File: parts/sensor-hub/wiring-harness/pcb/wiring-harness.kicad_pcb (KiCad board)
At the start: 2 copper layers, 95.7 x 51.7 mm, 20 parts, among them J1 Conn_01x01_Shielded

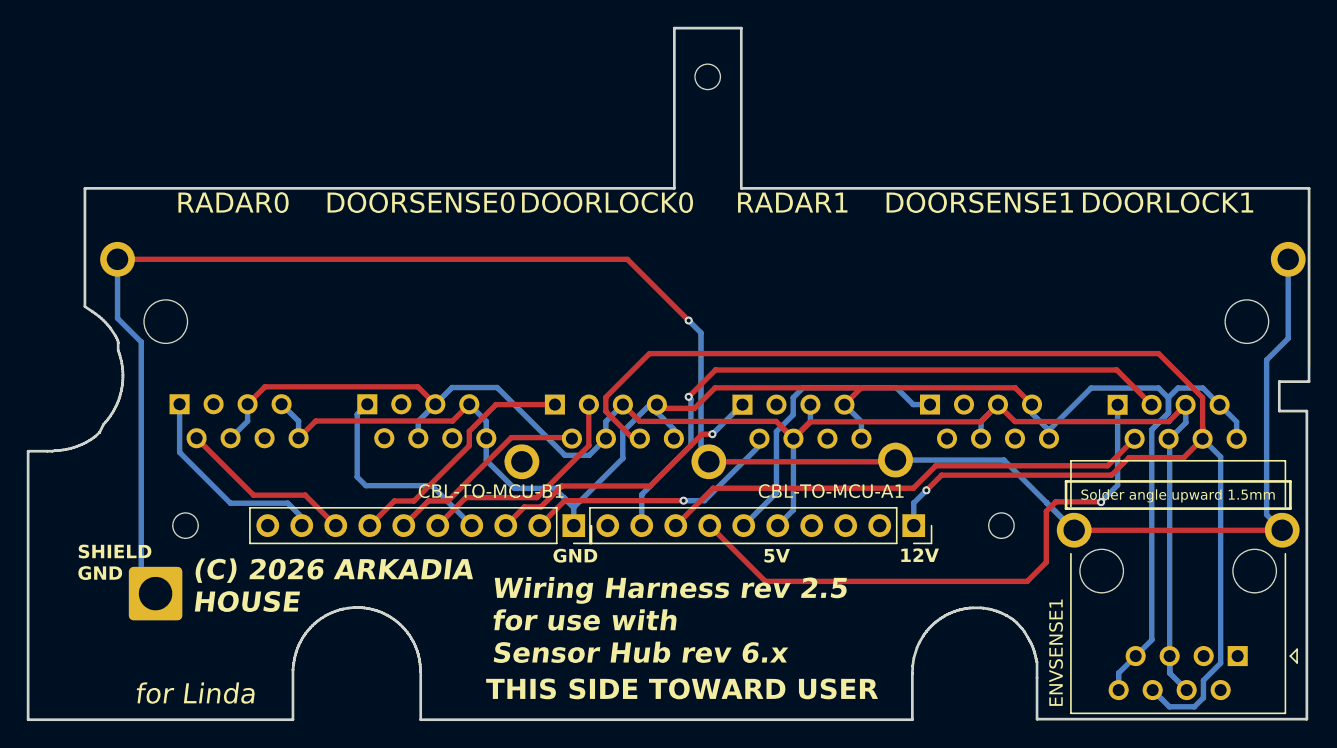
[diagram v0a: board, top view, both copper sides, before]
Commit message: tweak pcb layout to strengthen the supports.
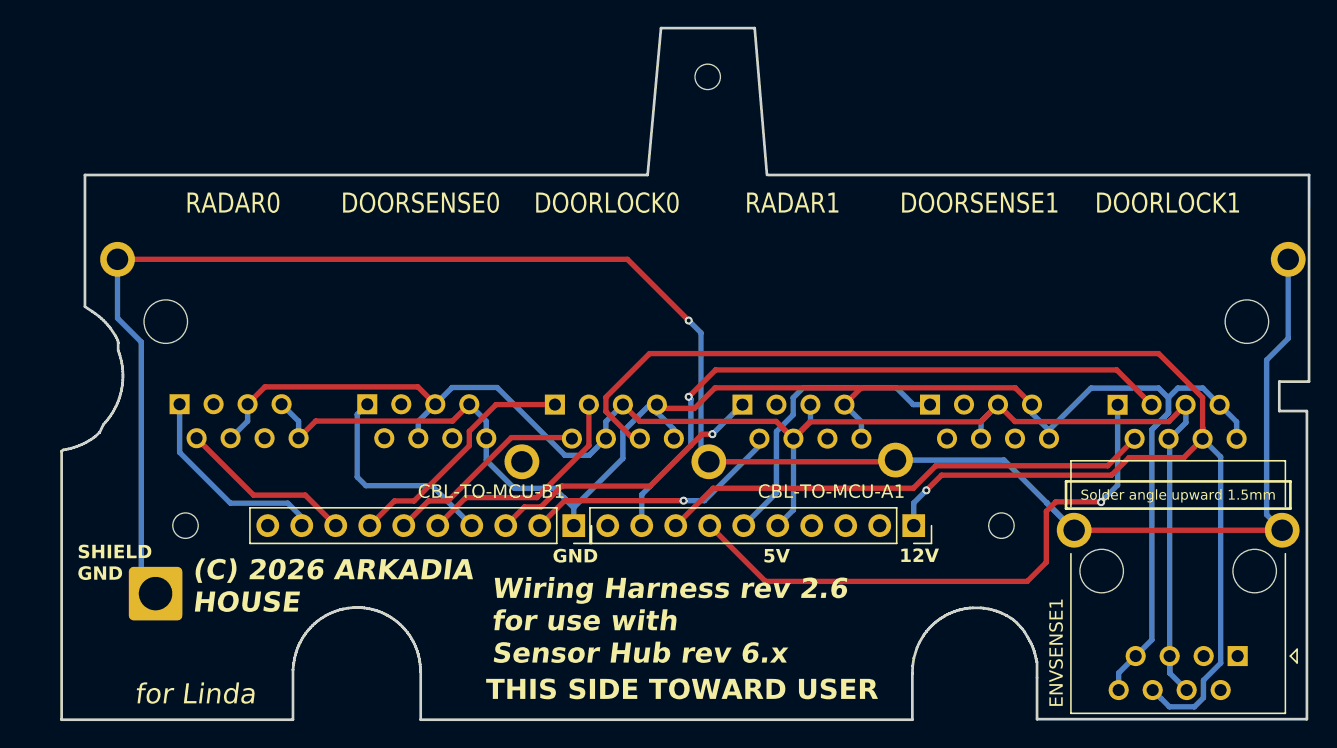
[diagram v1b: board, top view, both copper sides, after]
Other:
- board size 95.7 x 51.7 mm -> 93.2 x 51.7 mm
- board text added: "Wiring Harness rev 2.6 for use with Sensor Hub rev 6.x"
- board text removed: "Wiring Harness rev 2.5 for use with Sensor Hub rev 6.x"

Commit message: pcb revisions to update to better RJ45 jack, update QR code.
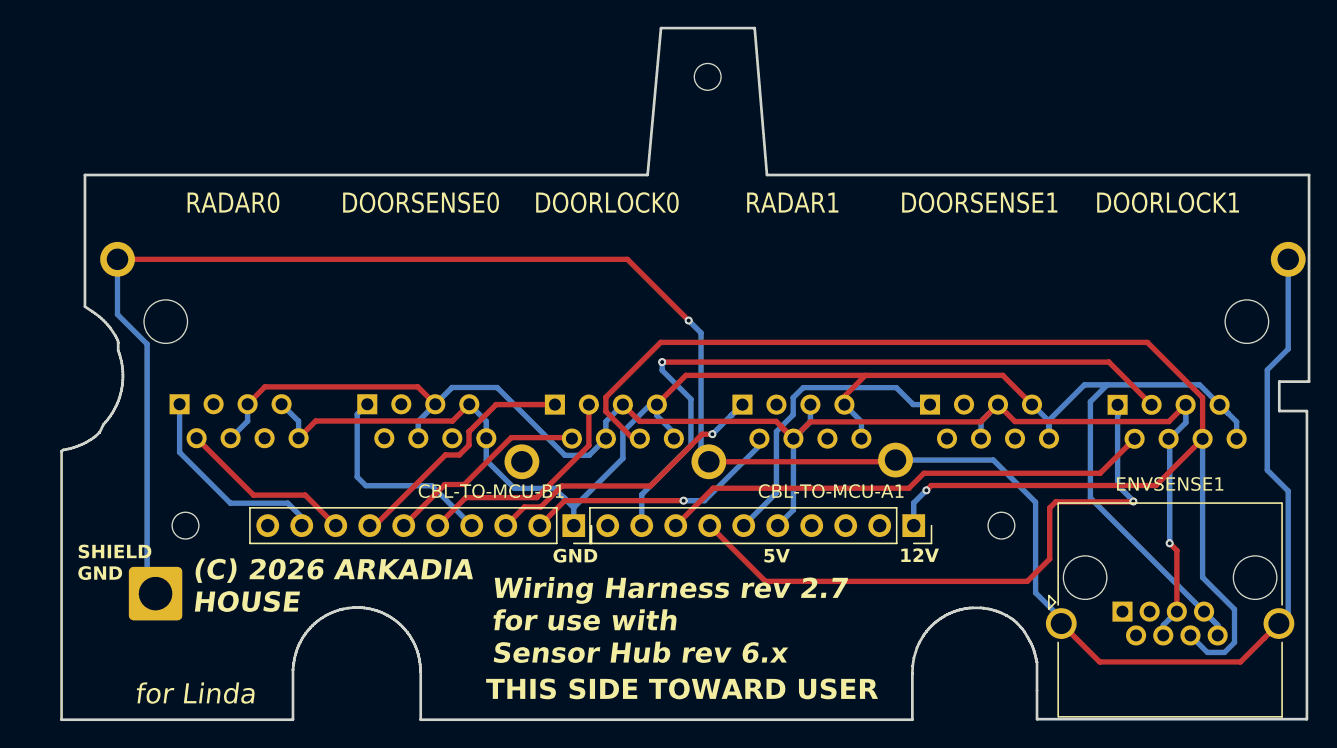
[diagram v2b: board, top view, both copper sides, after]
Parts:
- ENVSENSE1: footprint Connector_RJ:RJ45_Ninigi_GE -> Connector_RJ:RJ45_Amphenol_RJHSE5380
- moved ENVSENSE1 9.22 mm to (104.0, 93.7), turned to 0 degrees
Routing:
- net /SHIELD: track 151.3 -> 162.7 mm
- net /5V: track 123.5 -> 117.6 mm, vias 0 -> 1
- net /12V: track 105.9 -> 100.5 mm
- net Net-(CBL-TO-MCU-A1-DL1_UNLOCK): track 48.0 -> 52.2 mm
- net Net-(CBL-TO-MCU-A1-DL1_SENSE): track 43.5 -> 46.6 mm
- net Net-(CBL-TO-MCU-B1-R1_TXD_TO_RXD): track 21.4 -> 22.6 mm
- net Net-(CBL-TO-MCU-A1-DL1_LOCK): track 37.0 -> 37.7 mm
- net Net-(CBL-TO-MCU-B1-R1_RXD_TO_TXD): track 19.4 -> 18.9 mm
- net /GND: track 127.7 -> 127.2 mm
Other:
- outline, holes or cut-outs redrawn
- board text added: "Wiring Harness rev 2.7 for use with Sensor Hub rev 6.x"
- board text removed: "Solder angle upward 1.5mm"
- board text removed: "Wiring Harness rev 2.6 for use with Sensor Hub rev 6.x"
